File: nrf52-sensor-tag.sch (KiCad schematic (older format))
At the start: 20 parts, among them IC2 VEML6030, IC3 MS860702BA01-50, J3 Conn_01x07_Male, U1 MS88SF2

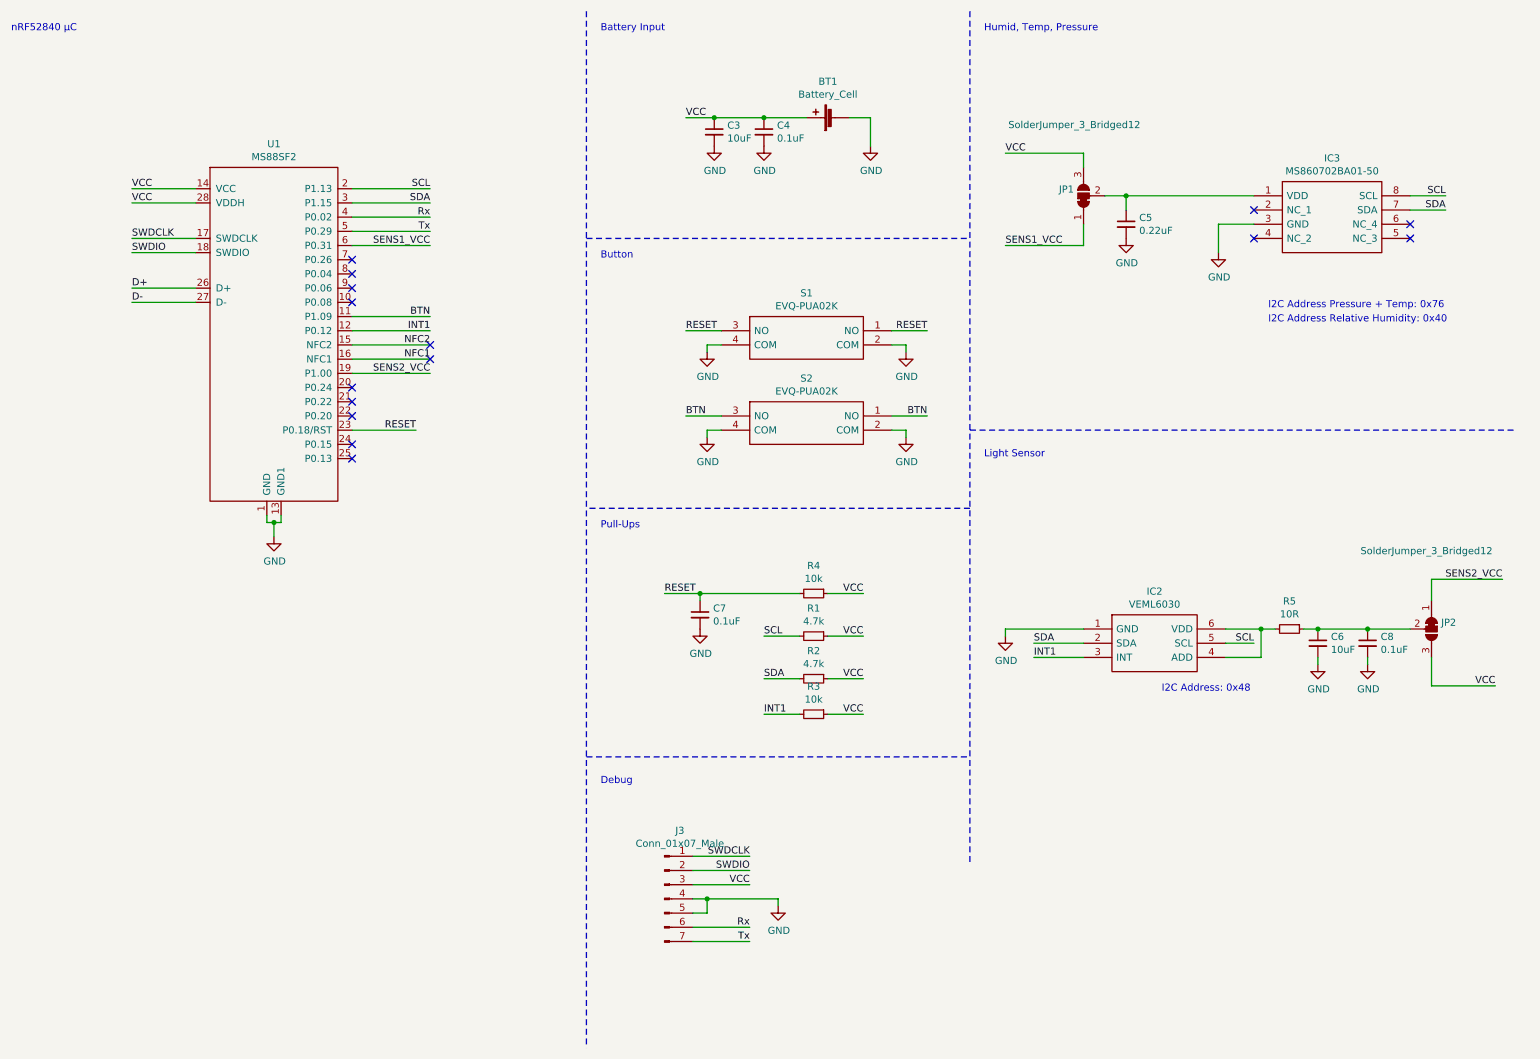
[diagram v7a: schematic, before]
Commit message: Removed unneseccary components because the battery is a very undisturbed source
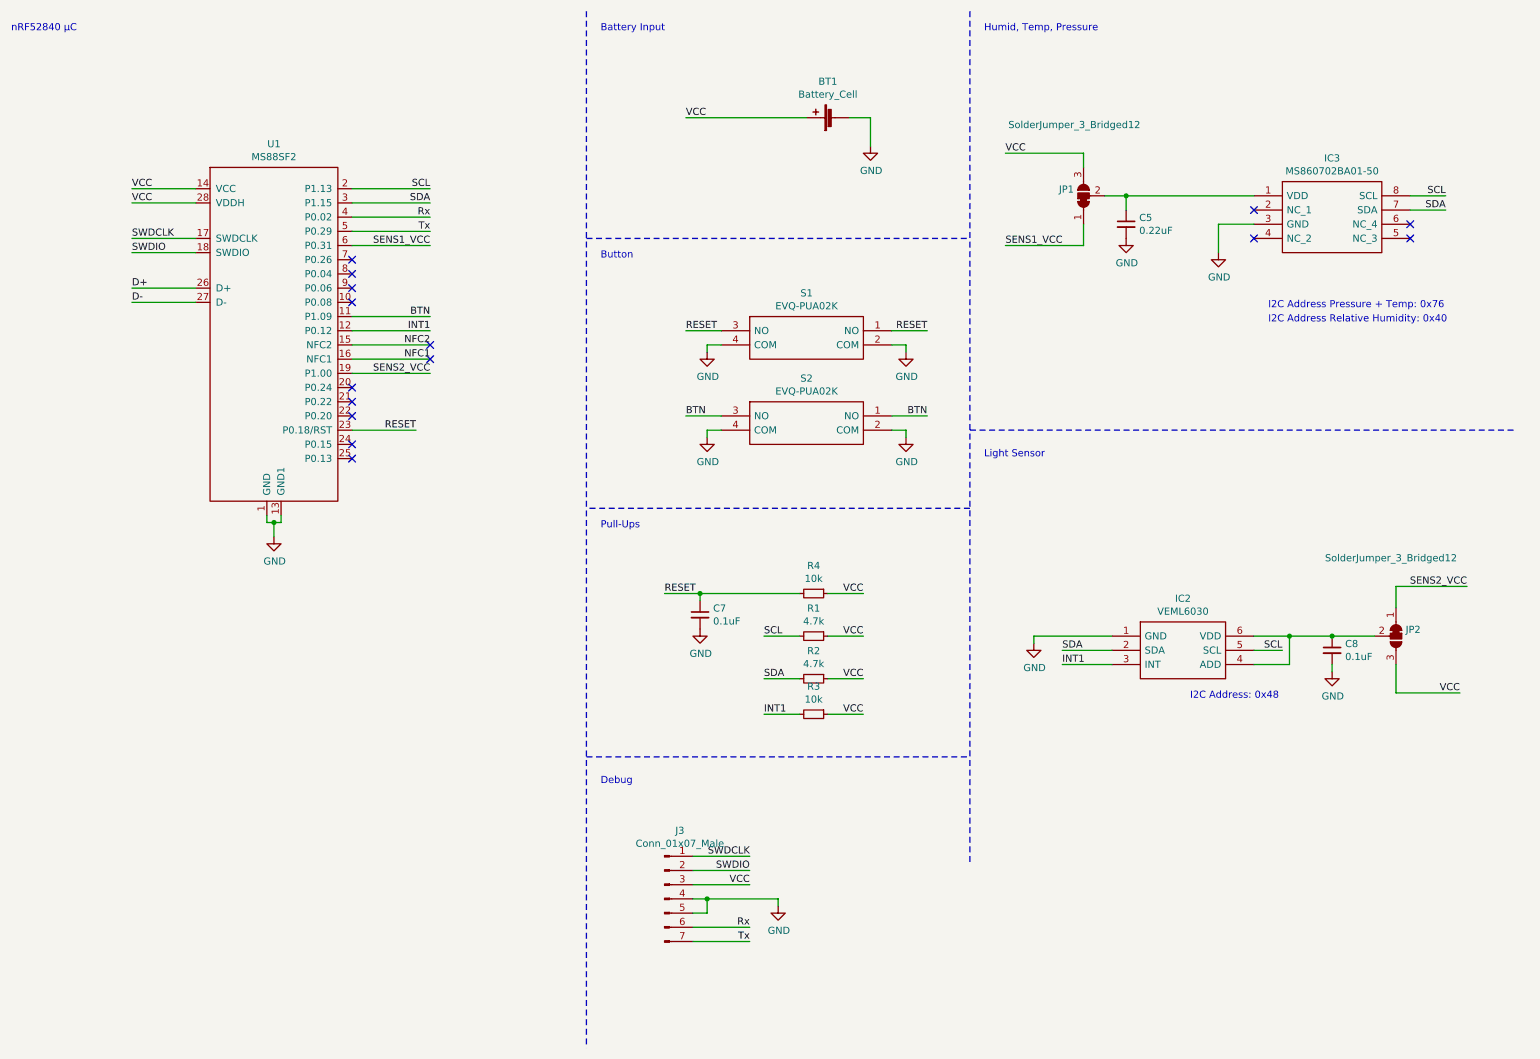
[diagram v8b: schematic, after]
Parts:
- removed C3, C6: 10uF, Capacitor_SMD:C_0603_1608Metric, symbol Device:C_Small
- removed C4: 0.1uF, Capacitor_SMD:C_0603_1608Metric, symbol Device:C_Small
- removed R5: 10R, Resistor_SMD:R_0603_1608Metric, symbol Device:R_Small
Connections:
- net at IC2.4 (ADD), IC2.6 (VDD): now also C8.1, JP2.2 (C)
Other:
- moved on the sheet: C8, IC2, JP2
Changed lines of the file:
@@
 Wire Wire Line
 	6600 4900 6350 4900
-Text Label 11100 4500 2    50   ~ 0
+Text Label 10850 4550 2    50   ~ 0
 SENS2_VCC
 Text Label 5900 5450 0    50   ~ 0
@@
 Text Notes 9450 2600 0    50   ~ 0
 I2C Address Pressure + Temp: 0x76
-Text Notes 8700 5300 0    50   ~ 0
+Text Notes 8900 5350 0    50   ~ 0
 I2C Address: 0x48
-$Comp
-L Device:C_Small C3
-U 1 1 60277C20
-P 5550 1350
-F 0 "C3" H 5642 1396 50  0000 L CNN
-F 1 "10uF" H 5642 1305 50  0000 L CNN
-F 2 "Capacitor_SMD:C_0603_1608Metric" H 5550 1350 50  0001 C CNN
-F 3 "~" H 5550 1350 50  0001 C CNN
-	1    5550 1350
-	1    0    0    -1
-$EndComp
-$Comp
-L Device:C_Small C4
-U 1 1 6027821B
-P 5900 1350
-F 0 "C4" H 5992 1396 50  0000 L CNN
-F 1 "0.1uF" H 5992 1305 50  0000 L CNN
-F 2 "Capacitor_SMD:C_0603_1608Metric" H 5900 1350 50  0001 C CNN
-F 3 "~" H 5900 1350 50  0001 C CNN
-	1    5900 1350
-	1    0    0    -1
-$EndComp
-Wire Wire Line
-	6200 1250 5900 1250
-Connection ~ 5550 1250
-Wire Wire Line
-	5550 1250 5350 1250
-Connection ~ 5900 1250
-Wire Wire Line
-	5900 1250 5550 1250
-$Comp
-L power:GND #PWR0109
-U 1 1 6027D829
-P 5550 1450
-F 0 "#PWR0109" H 5550 1200 50  0001 C CNN
-F 1 "GND" H 5555 1277 50  0000 C CNN
-F 2 "" H 5550 1450 50  0001 C CNN
-F 3 "" H 5550 1450 50  0001 C CNN
-	1    5550 1450
-	1    0    0    -1
-$EndComp
-$Comp
-L power:GND #PWR0110
-U 1 1 6027E10B
-P 5900 1450
-F 0 "#PWR0110" H 5900 1200 50  0001 C CNN
-F 1 "GND" H 5905 1277 50  0000 C CNN
-F 2 "" H 5900 1450 50  0001 C CNN
-F 3 "" H 5900 1450 50  0001 C CNN
-	1    5900 1450
-	1    0    0    -1
-$EndComp
 $Comp
 L power:GND #PWR0111
@@
 Wire Wire Line
 	3000 3050 3550 3050
-Text Label 11050 5250 2    50   ~ 0
+Text Label 10800 5300 2    50   ~ 0
 VCC
 Text Label 5800 6550 2    50   ~ 0
@@
 L VEML6030:VEML6030 IC2
 U 1 1 6023279F
-P 8150 4850
-F 0 "IC2" H 8650 5115 50  0000 C CNN
-F 1 "VEML6030" H 8650 5024 50  0000 C CNN
-F 2 "VEML6030:VEML6030" H 9000 4950 50  0001 L CNN
-F 3 "https://www.vishay.com/docs/84366/veml6030.pdf" H 9000 4850 50  0001 L CNN
-F 4 "VEML6030 Vishay, Ambient Light Sensor, Ambient Light to Digital Data I2C 6-Pin" H 9000 4750 50  0001 L CNN "Description"
-F 5 "0.87" H 9000 4650 50  0001 L CNN "Height"
-F 6 "Vishay" H 9000 4550 50  0001 L CNN "Manufacturer_Name"
-F 7 "VEML6030" H 9000 4450 50  0001 L CNN "Manufacturer_Part_Number"
-F 8 "78-VEML6030" H 9000 4350 50  0001 L CNN "Mouser Part Number"
-F 9 "https://www.mouser.co.uk/ProductDetail/Vishay-Semiconductors/VEML6030/?qs=oeTp6q%252Bm7GMZCCnCKRrv4g%3D%3D" H 9000 4250 50  0001 L CNN "Mouser Price/Stock"
-F 10 "VEML6030" H 9000 4150 50  0001 L CNN "Arrow Part Number"
-F 11 "https://www.arrow.com/en/products/veml6030/vishay" H 9000 4050 50  0001 L CNN "Arrow Price/Stock"
-	1    8150 4850
-	1    0    0    -1
-$EndComp
-Text Label 7800 5050 0    50   ~ 0
+P 8350 4900
+F 0 "IC2" H 8850 5165 50  0000 C CNN
+F 1 "VEML6030" H 8850 5074 50  0000 C CNN
+F 2 "VEML6030:VEML6030" H 9200 5000 50  0001 L CNN
+F 3 "https://www.vishay.com/docs/84366/veml6030.pdf" H 9200 4900 50  0001 L CNN
+F 4 "VEML6030 Vishay, Ambient Light Sensor, Ambient Light to Digital Data I2C 6-Pin" H 9200 4800 50  0001 L CNN "Description"
+F 5 "0.87" H 9200 4700 50  0001 L CNN "Height"
+F 6 "Vishay" H 9200 4600 50  0001 L CNN "Manufacturer_Name"
+F 7 "VEML6030" H 9200 4500 50  0001 L CNN "Manufacturer_Part_Number"
+F 8 "78-VEML6030" H 9200 4400 50  0001 L CNN "Mouser Part Number"
+F 9 "https://www.mouser.co.uk/ProductDetail/Vishay-Semiconductors/VEML6030/?qs=oeTp6q%252Bm7GMZCCnCKRrv4g%3D%3D" H 9200 4300 50  0001 L CNN "Mouser Price/Stock"
+F 10 "VEML6030" H 9200 4200 50  0001 L CNN "Arrow Part Number"
+F 11 "https://www.arrow.com/en/products/veml6030/vishay" H 9200 4100 50  0001 L CNN "Arrow Price/Stock"
+	1    8350 4900
+	1    0    0    -1
+$EndComp
+Text Label 8000 5100 0    50   ~ 0
 INT1
 Wire Wire Line
-	8150 5050 7800 5050
-Text Label 7800 4950 0    50   ~ 0
+	8350 5100 8000 5100
+Text Label 8000 5000 0    50   ~ 0
 SDA
-Text Label 9350 4950 2    50   ~ 0
+Text Label 9550 5000 2    50   ~ 0
 SCL
 Wire Wire Line
-	9150 4950 9350 4950
+	9350 5000 9550 5000
 $Comp
 L Device:C_Small C8
 U 1 1 6025B296
-P 10150 4950
-F 0 "C8" H 10242 4996 50  0000 L CNN
-F 1 "0.1uF" H 10242 4905 50  0000 L CNN
-F 2 "Capacitor_SMD:C_0603_1608Metric" H 10150 4950 50  0001 C CNN
-F 3 "~" H 10150 4950 50  0001 C CNN
-	1    10150 4950
-	1    0    0    -1
-$EndComp
-$Comp
-L Device:C_Small C6
-U 1 1 6025BDDE
-P 9800 4950
-F 0 "C6" H 9892 4996 50  0000 L CNN
-F 1 "10uF" H 9892 4905 50  0000 L CNN
-F 2 "Capacitor_SMD:C_0603_1608Metric" H 9800 4950 50  0001 C CNN
-F 3 "~" H 9800 4950 50  0001 C CNN
-	1    9800 4950
-	1    0    0    -1
-$EndComp
-Wire Wire Line
-	9800 4850 10150 4850
-$Comp
-L power:GND #PWR0102
-U 1 1 60266946
-P 9800 5100
-F 0 "#PWR0102" H 9800 4850 50  0001 C CNN
-F 1 "GND" H 9805 4927 50  0000 C CNN
-F 2 "" H 9800 5100 50  0001 C CNN
-F 3 "" H 9800 5100 50  0001 C CNN
-	1    9800 5100
+P 9900 5000
+F 0 "C8" H 9992 5046 50  0000 L CNN
+F 1 "0.1uF" H 9992 4955 50  0000 L CNN
+F 2 "Capacitor_SMD:C_0603_1608Metric" H 9900 5000 50  0001 C CNN
+F 3 "~" H 9900 5000 50  0001 C CNN
+	1    9900 5000
 	1    0    0    -1
 $EndComp
@@
 L power:GND #PWR0103
 U 1 1 60266FC1
-P 10150 5100
-F 0 "#PWR0103" H 10150 4850 50  0001 C CNN
-F 1 "GND" H 10155 4927 50  0000 C CNN
-F 2 "" H 10150 5100 50  0001 C CNN
-F 3 "" H 10150 5100 50  0001 C CNN
-	1    10150 5100
+P 9900 5150
+F 0 "#PWR0103" H 9900 4900 50  0001 C CNN
+F 1 "GND" H 9905 4977 50  0000 C CNN
+F 2 "" H 9900 5150 50  0001 C CNN
+F 3 "" H 9900 5150 50  0001 C CNN
+	1    9900 5150
 	1    0    0    -1
 $EndComp
@@
 L power:GND #PWR0104
 U 1 1 6026727A
-P 7600 4900
-F 0 "#PWR0104" H 7600 4650 50  0001 C CNN
-F 1 "GND" H 7605 4727 50  0000 C CNN
-F 2 "" H 7600 4900 50  0001 C CNN
-F 3 "" H 7600 4900 50  0001 C CNN
-	1    7600 4900
-	1    0    0    -1
-$EndComp
-Wire Wire Line
-	7800 4950 8150 4950
-Wire Wire Line
-	8150 4850 7600 4850
-Wire Wire Line
-	7600 4850 7600 4900
-Wire Wire Line
-	9800 5100 9800 5050
-Wire Wire Line
-	10150 5100 10150 5050
-$Comp
-L Device:R_Small R5
-U 1 1 60278CF3
-P 9600 4850
-F 0 "R5" V 9404 4850 50  0000 C CNN
-F 1 "10R" V 9495 4850 50  0000 C CNN
-F 2 "Resistor_SMD:R_0603_1608Metric" H 9600 4850 50  0001 C CNN
-F 3 "~" H 9600 4850 50  0001 C CNN
-	1    9600 4850
-	0    1    1    0
-$EndComp
-Wire Wire Line
-	9150 4850 9400 4850
-Wire Wire Line
-	9150 5050 9400 5050
-Wire Wire Line
-	9400 5050 9400 4850
-Wire Wire Line
-	9500 4850 9400 4850
-Connection ~ 9400 4850
-Wire Wire Line
-	9700 4850 9800 4850
-Connection ~ 9800 4850
+P 7800 4950
+F 0 "#PWR0104" H 7800 4700 50  0001 C CNN
+F 1 "GND" H 7805 4777 50  0000 C CNN
+F 2 "" H 7800 4950 50  0001 C CNN
+F 3 "" H 7800 4950 50  0001 C CNN
+	1    7800 4950
+	1    0    0    -1
+$EndComp
+Wire Wire Line
+	8000 5000 8350 5000
+Wire Wire Line
+	8350 4900 7800 4900
+Wire Wire Line
+	7800 4900 7800 4950
+Wire Wire Line
+	9900 5150 9900 5100
+Wire Wire Line
+	9350 4900 9600 4900
+Wire Wire Line
+	9350 5100 9600 5100
+Wire Wire Line
+	9600 5100 9600 4900
+Connection ~ 9600 4900
 Text Label 7600 1500 0    50   ~ 0
 VCC
@@
 L Jumper:SolderJumper_3_Bridged12 JP2
 U 1 1 603AE514
-P 10600 4850
-F 0 "JP2" V 10554 4918 50  0000 L CNN
-F 1 "SolderJumper_3_Bridged12" V 10050 4350 50  0000 L CNN
-F 2 "Jumper:SolderJumper-3_P1.3mm_Bridged12_RoundedPad1.0x1.5mm" H 10600 4850 50  0001 C CNN
-F 3 "~" H 10600 4850 50  0001 C CNN
-	1    10600 4850
+P 10350 4900
+F 0 "JP2" V 10304 4968 50  0000 L CNN
+F 1 "SolderJumper_3_Bridged12" V 9800 4400 50  0000 L CNN
+F 2 "Jumper:SolderJumper-3_P1.3mm_Bridged12_RoundedPad1.0x1.5mm" H 10350 4900 50  0001 C CNN
+F 3 "~" H 10350 4900 50  0001 C CNN
+	1    10350 4900
 	0    1    1    0
 $EndComp
@@
 	8150 1500 7600 1500
 Wire Wire Line
-	10450 4850 10150 4850
-Connection ~ 10150 4850
-Wire Wire Line
-	11100 4500 10600 4500
-Wire Wire Line
-	10600 4500 10600 4650
-Wire Wire Line
-	11050 5250 10600 5250
-Wire Wire Line
-	10600 5050 10600 5250
+	10200 4900 9900 4900
+Wire Wire Line
+	10850 4550 10350 4550
+Wire Wire Line
+	10350 4550 10350 4700
+Wire Wire Line
+	10800 5300 10350 5300
+Wire Wire Line
+	10350 5100 10350 5300
 NoConn ~ 3000 2450
 NoConn ~ 3000 2350
 NoConn ~ 3000 2250
+Wire Wire Line
+	9600 4900 9900 4900
+Connection ~ 9900 4900
+Wire Wire Line
+	5350 1250 6200 1250
 $EndSCHEMATC
